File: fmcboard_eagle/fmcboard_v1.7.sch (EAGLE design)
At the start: 294 parts, among them IC1 OPA699ID, IC10 LM358, IC11 7805DT, IC12 SN74AUC2G66DCTR, IC13 SN74AUC2G66DCTR, IC14 SN74AUC2G66DCTR, IC15 SN74AUC2G66DCTR, IC16 DAC7578SPWR, IC17 SN74AUC2G66DCTR, IC18 SN74AUC2G66DCTR, IC19 SN74AUC2G66DCTR, IC2 DAC7578SPWR, IC20 SN74AUC2G66DCTR, IC21 74AUP2GU04GW, IC22 74AUP2GU04GW, IC23 74AUP2GU04GW, IC24 74AUP2GU04GW, IC25 MC7905ACD2TR4G, IC26 AMS1117-1.8, IC27 LM358, IC28 SN74AUC2G66DCTR, IC29 LM337KVURG3, IC3 LTC6229IMS8E#TRPBF, IC30 SN74AUC2G66DCTR, IC31 SN74AUC2G66DCTR, IC32 SN74AUC2G66DCTR, IC33 LTC6229IMS8E#TRPBF, IC34 74AUP2GU04GW, IC35 74AUP2GU04GW, IC36 TPS5430DDAR, IC37 TPS5430DDAR, IC38 LTC6229IMS8E#TRPBF, IC4 OPA695IDR, IC5 LTC6229IMS8E#TRPBF, IC6 OPA695IDR, IC7 OPA699ID, IC8 LM358, IC9 LM358, J1 4p-2.54, J13 4p-2.54, J2 ASP-134604-01, J3 2X4P-2.54, J4 2X4P-2.54, J5 4p-2.54

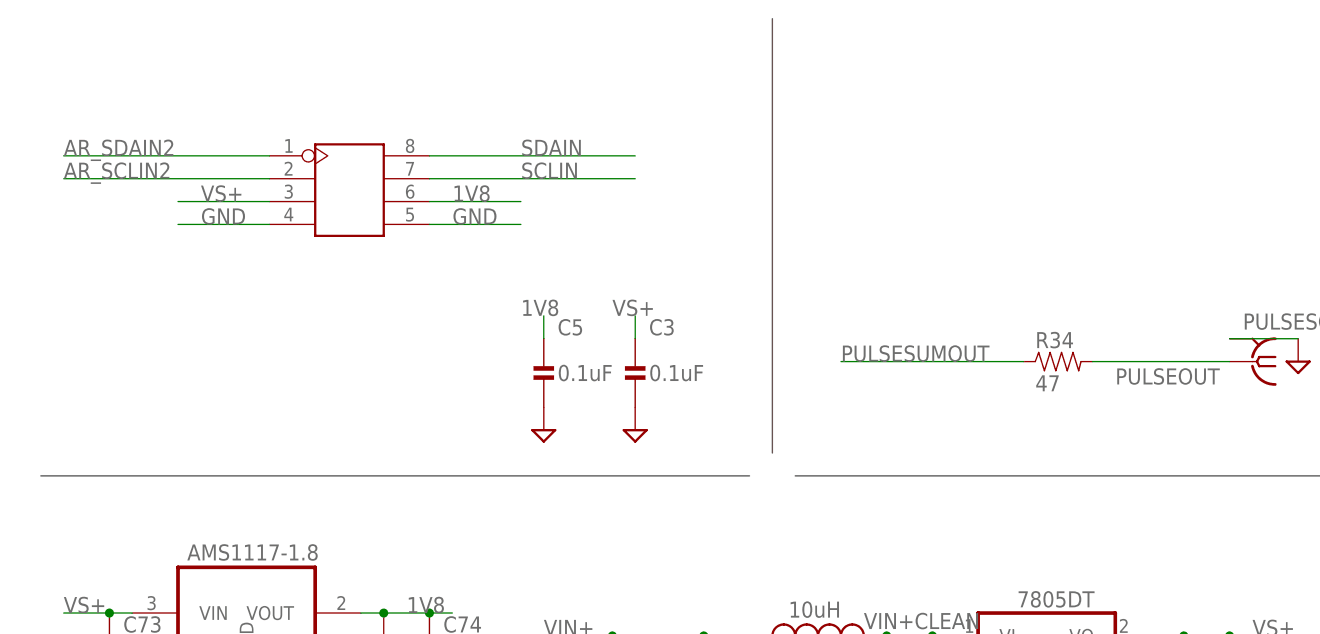
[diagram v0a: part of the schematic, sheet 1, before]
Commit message: add level shifting
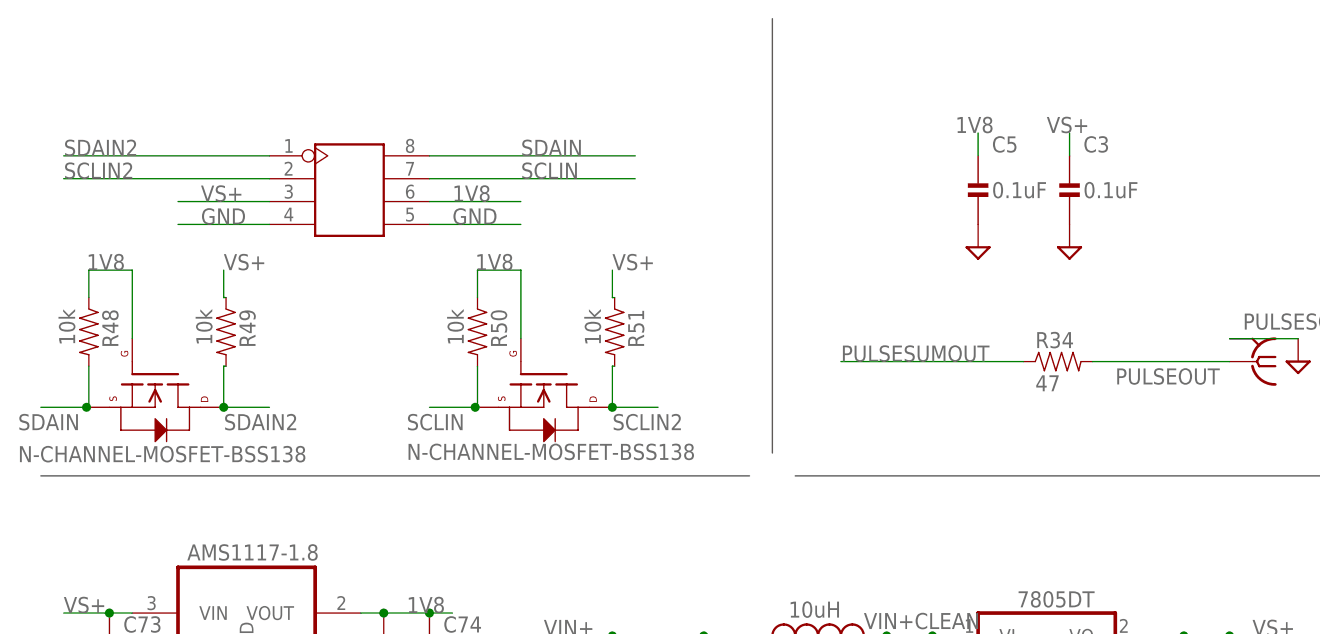
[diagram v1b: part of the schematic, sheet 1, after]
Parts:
- added R48, R49, R50, R51: 10k, passives:RESISTOR0402_RES
- added U$1, U$2: N-CHANNEL-MOSFET-BSS138, GeekAmmo:N-CHANNEL-MOSFET-BSS138
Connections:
- removed net AR_SCLIN2: IC16.SCL, IC2.SCL, J4.2
- removed net AR_SDAIN2: IC16.SDA, IC2.SDA, J4.1
- new net SCLIN2: IC16.SCL, IC2.SCL, J4.2, R51.2, U$2.D
- new net SDAIN2: IC16.SDA, IC2.SDA, J4.1, R49.2, U$1.D
- net 1V8: now also R48.1, R50.1, U$1.G, U$2.G
- net SCLIN: now also R50.2, U$2.S
- net SDAIN: now also R48.2, U$1.S
- net VS+: now also R49.1, R51.1
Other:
- moved on the sheet: C3, C5
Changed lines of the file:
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@@
 <part name="J3" library="Seeed-Connector" library_urn="urn:adsk.eagle:library:478" deviceset="DIP-BLACK-FEMALE-HEADER(2X4P-2.54)" device="" package3d_urn="urn:adsk.eagle:package:33148/1" value="2X4P-2.54"/>
 <part name="J4" library="Seeed-Connector" library_urn="urn:adsk.eagle:library:478" deviceset="DIP-BLACK-FEMALE-HEADER(2X4P-2.54)" device="" package3d_urn="urn:adsk.eagle:package:33148/1" value="2X4P-2.54"/>
+<part name="U$1" library="GeekAmmo" deviceset="N-CHANNEL-MOSFET" device="-BSS138"/>
+<part name="U$2" library="GeekAmmo" deviceset="N-CHANNEL-MOSFET" device="-BSS138"/>
+<part name="R48" library="passives" deviceset="RESISTOR" device="0402_RES" value="10k"/>
+<part name="R49" library="passives" deviceset="RESISTOR" device="0402_RES" value="10k"/>
+<part name="R50" library="passives" deviceset="RESISTOR" device="0402_RES" value="10k"/>
+<part name="R51" library="passives" deviceset="RESISTOR" device="0402_RES" value="10k"/>
 </parts>
 <sheets>
@@
 </plain>
 <instances>
-<instance part="C3" gate="G$1" x="-7.62" y="68.58" smashed="yes">
-<attribute name="NAME" x="-6.096" y="71.501" size="1.778" layer="95"/>
-<attribute name="VALUE" x="-6.096" y="66.421" size="1.778" layer="96"/>
-</instance>
-<instance part="C5" gate="G$1" x="-17.78" y="68.58" smashed="yes">
-<attribute name="NAME" x="-16.256" y="71.501" size="1.778" layer="95"/>
-<attribute name="VALUE" x="-16.256" y="66.421" size="1.778" layer="96"/>
+<instance part="C3" gate="G$1" x="40.64" y="88.9" smashed="yes">
+<attribute name="NAME" x="42.164" y="91.821" size="1.778" layer="95"/>
+<attribute name="VALUE" x="42.164" y="86.741" size="1.778" layer="96"/>
+</instance>
+<instance part="C5" gate="G$1" x="30.48" y="88.9" smashed="yes">
+<attribute name="NAME" x="32.004" y="91.821" size="1.778" layer="95"/>
+<attribute name="VALUE" x="32.004" y="86.741" size="1.778" layer="96"/>
 </instance>
 <instance part="C7" gate="G$1" x="96.52" y="30.48" smashed="yes">
@@
 <instance part="SUPPLY11" gate="GND" x="76.2" y="22.86" smashed="yes"/>
 <instance part="SUPPLY12" gate="GND" x="86.36" y="22.86" smashed="yes"/>
-<instance part="SUPPLY13" gate="GND" x="-7.62" y="60.96" smashed="yes"/>
-<instance part="SUPPLY14" gate="GND" x="-17.78" y="60.96" smashed="yes"/>
+<instance part="SUPPLY13" gate="GND" x="40.64" y="81.28" smashed="yes"/>
+<instance part="SUPPLY14" gate="GND" x="30.48" y="81.28" smashed="yes"/>
 <instance part="SUPPLY16" gate="GND" x="81.28" y="-7.62" smashed="yes"/>
 <instance part="SUPPLY17" gate="GND" x="88.9" y="-7.62" smashed="yes"/>
@@
 <instance part="J3" gate="G$1" x="123.444" y="-3.81" smashed="yes"/>
 <instance part="J4" gate="G$1" x="-39.37" y="87.63" smashed="yes"/>
+<instance part="U$1" gate="G$1" x="-60.96" y="66.04" smashed="yes" rot="R270">
+<attribute name="VALUE" x="-76.2" y="57.404" size="1.778" layer="96"/>
+</instance>
+<instance part="U$2" gate="G$1" x="-17.78" y="66.04" smashed="yes" rot="R270">
+<attribute name="VALUE" x="-33.02" y="57.658" size="1.778" layer="96"/>
+</instance>
+<instance part="R48" gate="G$1" x="-68.326" y="70.612" smashed="yes" rot="R270">
+<attribute name="NAME" x="-66.8274" y="74.422" size="1.778" layer="95" rot="R270"/>
+<attribute name="VALUE" x="-71.628" y="74.422" size="1.778" layer="96" rot="R270"/>
+</instance>
+<instance part="R49" gate="G$1" x="-53.086" y="70.612" smashed="yes" rot="R270">
+<attribute name="NAME" x="-51.5874" y="74.422" size="1.778" layer="95" rot="R270"/>
+<attribute name="VALUE" x="-56.388" y="74.422" size="1.778" layer="96" rot="R270"/>
+</instance>
+<instance part="R50" gate="G$1" x="-25.146" y="70.612" smashed="yes" rot="R270">
+<attribute name="NAME" x="-23.6474" y="74.422" size="1.778" layer="95" rot="R270"/>
+<attribute name="VALUE" x="-28.448" y="74.422" size="1.778" layer="96" rot="R270"/>
+</instance>
+<instance part="R51" gate="G$1" x="-9.906" y="70.612" smashed="yes" rot="R270">
+<attribute name="NAME" x="-8.4074" y="74.422" size="1.778" layer="95" rot="R270"/>
+<attribute name="VALUE" x="-13.208" y="74.422" size="1.778" layer="96" rot="R270"/>
+</instance>
 </instances>
 <busses>
@@
 <net name="1V8" class="1">
 <segment>
-<label x="-20.32" y="73.66" size="1.778" layer="95"/>
+<label x="27.94" y="93.98" size="1.778" layer="95"/>
 <pinref part="C5" gate="G$1" pin="1"/>
-<wire x1="-17.78" y1="71.12" x2="-17.78" y2="73.66" width="0.1524" layer="91"/>
+<wire x1="30.48" y1="91.44" x2="30.48" y2="93.98" width="0.1524" layer="91"/>
 </segment>
 <segment>
@@
 <label x="-27.94" y="86.36" size="1.778" layer="95"/>
 </segment>
+<segment>
+<pinref part="R48" gate="G$1" pin="1"/>
+<wire x1="-68.326" y1="75.692" x2="-68.326" y2="78.74" width="0.1524" layer="91"/>
+<pinref part="U$1" gate="G$1" pin="G"/>
+<wire x1="-68.326" y1="78.74" x2="-63.5" y2="78.74" width="0.1524" layer="91"/>
+<wire x1="-63.5" y1="78.74" x2="-63.5" y2="71.12" width="0.1524" layer="91"/>
+<label x="-68.58" y="78.74" size="1.778" layer="95"/>
+</segment>
+<segment>
+<pinref part="R50" gate="G$1" pin="1"/>
+<wire x1="-25.146" y1="75.692" x2="-25.146" y2="78.74" width="0.1524" layer="91"/>
+<wire x1="-25.146" y1="78.74" x2="-20.32" y2="78.74" width="0.1524" layer="91"/>
+<pinref part="U$2" gate="G$1" pin="G"/>
+<wire x1="-20.32" y1="78.74" x2="-20.32" y2="71.12" width="0.1524" layer="91"/>
+<label x="-25.4" y="78.74" size="1.778" layer="95"/>
+</segment>
 </net>
 <net name="3V3" class="1">
@@
 <net name="VS+" class="1">
 <segment>
-<label x="-10.16" y="73.66" size="1.778" layer="95"/>
+<label x="38.1" y="93.98" size="1.778" layer="95"/>
 <pinref part="C3" gate="G$1" pin="1"/>
-<wire x1="-7.62" y1="73.66" x2="-7.62" y2="71.12" width="0.1524" layer="91"/>
+<wire x1="40.64" y1="93.98" x2="40.64" y2="91.44" width="0.1524" layer="91"/>
 </segment>
 <segment>
@@
 <label x="-55.88" y="86.36" size="1.778" layer="95"/>
 </segment>
+<segment>
+<pinref part="R49" gate="G$1" pin="1"/>
+<wire x1="-53.086" y1="75.692" x2="-53.34" y2="75.692" width="0.1524" layer="91"/>
+<wire x1="-53.34" y1="75.692" x2="-53.34" y2="78.74" width="0.1524" layer="91"/>
+<label x="-53.34" y="78.74" size="1.778" layer="95"/>
+</segment>
+<segment>
+<pinref part="R51" gate="G$1" pin="1"/>
+<wire x1="-9.906" y1="75.692" x2="-10.16" y2="75.692" width="0.1524" layer="91"/>
+<wire x1="-10.16" y1="75.692" x2="-10.16" y2="78.74" width="0.1524" layer="91"/>
+<label x="-10.16" y="78.74" size="1.778" layer="95"/>
+</segment>
 </net>
 <net name="VS-" class="1">
@@
 <pinref part="J4" gate="G$1" pin="8"/>
 </segment>
+<segment>
+<pinref part="U$1" gate="G$1" pin="S"/>
+<pinref part="R48" gate="G$1" pin="2"/>
+<wire x1="-68.58" y1="63.5" x2="-68.326" y2="63.5" width="0.1524" layer="91"/>
+<wire x1="-68.326" y1="63.5" x2="-68.326" y2="68.072" width="0.1524" layer="91"/>
+<wire x1="-68.58" y1="63.5" x2="-73.66" y2="63.5" width="0.1524" layer="91"/>
+<junction x="-68.58" y="63.5"/>
+<label x="-76.2" y="60.96" size="1.778" layer="95"/>
+</segment>
 </net>
 <net name="SCLIN" class="0">
@@
 <label x="-20.32" y="88.9" size="1.778" layer="95"/>
 <pinref part="J4" gate="G$1" pin="7"/>
+</segment>
+<segment>
+<pinref part="U$2" gate="G$1" pin="S"/>
+<pinref part="R50" gate="G$1" pin="2"/>
+<wire x1="-25.4" y1="63.5" x2="-25.146" y2="63.5" width="0.1524" layer="91"/>
+<wire x1="-25.146" y1="63.5" x2="-25.146" y2="68.072" width="0.1524" layer="91"/>
+<junction x="-25.4" y="63.5"/>
+<wire x1="-25.4" y1="63.5" x2="-30.48" y2="63.5" width="0.1524" layer="91"/>
+<label x="-33.02" y="60.96" size="1.778" layer="95"/>
 </segment>
 </net>
@@
 </segment>
 </net>
-<net name="AR_SDAIN2" class="0">
+<net name="SDAIN2" class="0">
 <segment>
 <wire x1="-48.26" y1="91.44" x2="-71.12" y2="91.44" width="0.1524" layer="91"/>
@@
 <pinref part="J4" gate="G$1" pin="1"/>
 </segment>
-</net>
-<net name="AR_SCLIN2" class="0">
+<segment>
+<pinref part="R49" gate="G$1" pin="2"/>
+<pinref part="U$1" gate="G$1" pin="D"/>
+<wire x1="-53.086" y1="68.072" x2="-53.34" y2="68.072" width="0.1524" layer="91"/>
+<wire x1="-53.34" y1="68.072" x2="-53.34" y2="63.5" width="0.1524" layer="91"/>
+<junction x="-53.34" y="63.5"/>
+<wire x1="-53.34" y1="63.5" x2="-48.26" y2="63.5" width="0.1524" layer="91"/>
+<label x="-53.34" y="60.96" size="1.778" layer="95"/>
+</segment>
+</net>
+<net name="SCLIN2" class="0">
 <segment>
 <wire x1="-48.26" y1="88.9" x2="-71.12" y2="88.9" width="0.1524" layer="91"/>
 <label x="-71.12" y="88.9" size="1.778" layer="95"/>
 <pinref part="J4" gate="G$1" pin="2"/>
+</segment>
+<segment>
+<pinref part="R51" gate="G$1" pin="2"/>
+<pinref part="U$2" gate="G$1" pin="D"/>
+<wire x1="-9.906" y1="68.072" x2="-10.16" y2="68.072" width="0.1524" layer="91"/>
+<wire x1="-10.16" y1="68.072" x2="-10.16" y2="63.5" width="0.1524" layer="91"/>
+<junction x="-10.16" y="63.5"/>
+<wire x1="-10.16" y1="63.5" x2="-5.08" y2="63.5" width="0.1524" layer="91"/>
+<label x="-10.16" y="60.96" size="1.778" layer="95"/>
 </segment>
 </net>
@@
 </segment>
 </net>
-<net name="AR_SCLIN2" class="0">
+<net name="SCLIN2" class="0">
 <segment>
 <pinref part="IC2" gate="G$1" pin="SCL"/>
@@
 </segment>
 </net>
-<net name="AR_SDAIN2" class="0">
+<net name="SDAIN2" class="0">
 <segment>
 <pinref part="IC2" gate="G$1" pin="SDA"/>

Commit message: v1.7
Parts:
- U$1, U$2: JLC_ROTATION (none) -> 270; LCSC (none) -> C5190146
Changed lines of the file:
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@@
 <part name="J3" library="Seeed-Connector" library_urn="urn:adsk.eagle:library:478" deviceset="DIP-BLACK-FEMALE-HEADER(2X4P-2.54)" device="" package3d_urn="urn:adsk.eagle:package:33148/1" value="2X4P-2.54"/>
 <part name="J4" library="Seeed-Connector" library_urn="urn:adsk.eagle:library:478" deviceset="DIP-BLACK-FEMALE-HEADER(2X4P-2.54)" device="" package3d_urn="urn:adsk.eagle:package:33148/1" value="2X4P-2.54"/>
-<part name="U$1" library="GeekAmmo" deviceset="N-CHANNEL-MOSFET" device="-BSS138"/>
-<part name="U$2" library="GeekAmmo" deviceset="N-CHANNEL-MOSFET" device="-BSS138"/>
+<part name="U$1" library="GeekAmmo" deviceset="N-CHANNEL-MOSFET" device="-BSS138">
+<attribute name="JLC_ROTATION" value="270"/>
+<attribute name="LCSC" value="C5190146"/>
+</part>
+<part name="U$2" library="GeekAmmo" deviceset="N-CHANNEL-MOSFET" device="-BSS138">
+<attribute name="JLC_ROTATION" value="270"/>
+<attribute name="LCSC" value="C5190146"/>
+</part>
 <part name="R48" library="passives" deviceset="RESISTOR" device="0402_RES" value="10k"/>
 <part name="R49" library="passives" deviceset="RESISTOR" device="0402_RES" value="10k"/>
@@
 <instance part="U$1" gate="G$1" x="-60.96" y="66.04" smashed="yes" rot="R270">
 <attribute name="VALUE" x="-76.2" y="57.404" size="1.778" layer="96"/>
+<attribute name="LCSC" x="-60.96" y="66.04" size="1.778" layer="96" rot="R270" display="off"/>
+<attribute name="JLC_ROTATION" x="-60.96" y="66.04" size="1.778" layer="96" rot="R270" display="off"/>
 </instance>
 <instance part="U$2" gate="G$1" x="-17.78" y="66.04" smashed="yes" rot="R270">
 <attribute name="VALUE" x="-33.02" y="57.658" size="1.778" layer="96"/>
+<attribute name="LCSC" x="-17.78" y="66.04" size="1.778" layer="96" rot="R270" display="off"/>
+<attribute name="JLC_ROTATION" x="-17.78" y="66.04" size="1.778" layer="96" rot="R270" display="off"/>
 </instance>
 <instance part="R48" gate="G$1" x="-68.326" y="70.612" smashed="yes" rot="R270">

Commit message: caps
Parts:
- added C118: 0.1uF, passives:CAPACITOR0402_CAP
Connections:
- net 1V8: now also C118.1
- net GND: now also C118.2
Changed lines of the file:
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@@
 <part name="R50" library="passives" deviceset="RESISTOR" device="0402_RES" value="10k"/>
 <part name="R51" library="passives" deviceset="RESISTOR" device="0402_RES" value="10k"/>
+<part name="C118" library="passives" deviceset="CAPACITOR" device="0402_CAP" value="0.1uF"/>
+<part name="SUPPLY24" library="supply2" library_urn="urn:adsk.eagle:library:372" deviceset="GND" device=""/>
 </parts>
 <sheets>
@@
 <attribute name="VALUE" x="-13.208" y="74.422" size="1.778" layer="96" rot="R270"/>
 </instance>
+<instance part="C118" gate="G$1" x="106.68" y="30.48" smashed="yes">
+<attribute name="NAME" x="108.204" y="33.401" size="1.778" layer="95"/>
+<attribute name="VALUE" x="108.204" y="28.321" size="1.778" layer="96"/>
+</instance>
+<instance part="SUPPLY24" gate="GND" x="106.68" y="22.86" smashed="yes"/>
 </instances>
 <busses>
@@
 <label x="-27.94" y="83.82" size="1.778" layer="95"/>
 </segment>
+<segment>
+<pinref part="SUPPLY24" gate="GND" pin="GND"/>
+<pinref part="C118" gate="G$1" pin="2"/>
+</segment>
 </net>
 <net name="1V8" class="1">
@@
 <label x="-25.4" y="78.74" size="1.778" layer="95"/>
 </segment>
+<segment>
+<pinref part="C118" gate="G$1" pin="1"/>
+<wire x1="106.68" y1="33.02" x2="106.68" y2="40.64" width="0.1524" layer="91"/>
+<label x="104.14" y="38.1" size="1.778" layer="95"/>
+</segment>
 </net>
